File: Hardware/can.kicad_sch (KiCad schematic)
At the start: 9 parts, among them U2 SN65HVD230

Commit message: Crosshair V1.0
New pyro connectors, silkscreen sorted, mostly connected properly + cool new name and image
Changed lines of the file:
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@@
 (kicad_sch
-	(version 20231120)
+	(version 20250114)
 	(generator "eeschema")
-	(generator_version "8.0")
+	(generator_version "9.0")
 	(paper "A4")
 	(junction
@@
 	(label "Vref"
 		(at 124.46 90.17 180)
-		(fields_autoplaced yes)
 		(effects
 			(font
@@
 	(label "Vref"
 		(at 153.67 88.9 180)
-		(fields_autoplaced yes)
 		(effects
 			(font
@@
 		(shape input)
 		(at 111.76 87.63 180)
-		(fields_autoplaced yes)
 		(effects
 			(font
@@
 		(shape bidirectional)
 		(at 175.26 80.01 0)
-		(fields_autoplaced yes)
 		(effects
 			(font
@@
 		(shape output)
 		(at 111.76 85.09 180)
-		(fields_autoplaced yes)
 		(effects
 			(font
@@
 		(shape bidirectional)
 		(at 190.5 97.79 0)
-		(fields_autoplaced yes)
 		(effects
 			(font
@@
 		(shape bidirectional)
 		(at 190.5 80.01 0)
-		(fields_autoplaced yes)
 		(effects
 			(font
@@
 		(shape bidirectional)
 		(at 175.26 97.79 0)
-		(fields_autoplaced yes)
-		(effects
-			(font
+		(effects
+			(font

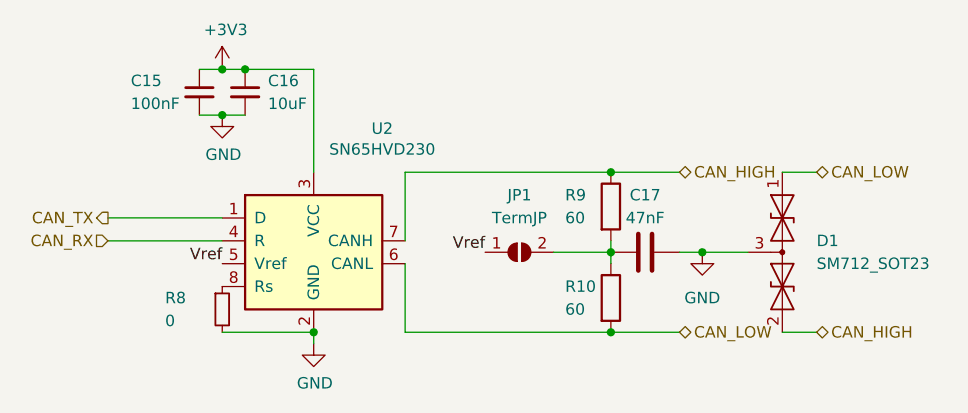
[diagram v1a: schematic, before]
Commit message: More V2 changes
Mainly changed to use Ω symbol for resistors. Fixed the CDC pin for the buck boost
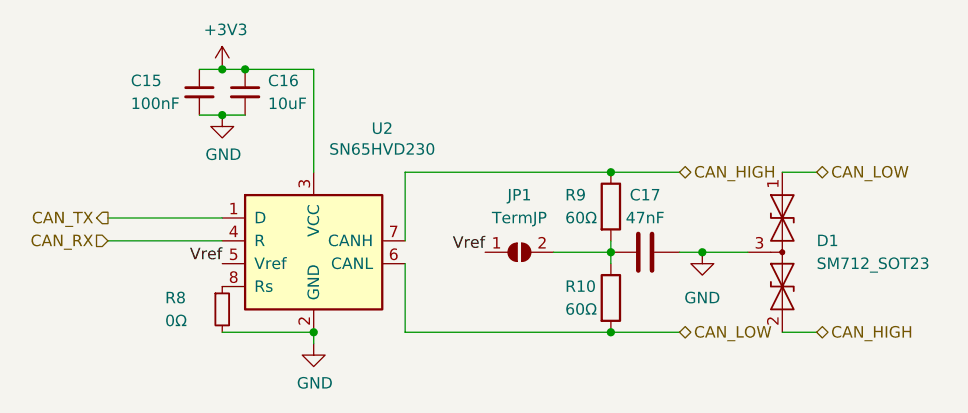
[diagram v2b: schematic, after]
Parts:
- R10, R9: value 60 -> 60Ω
- R8: value 0 -> 0Ω
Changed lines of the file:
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@@
 			)
 		)
-		(property "Value" "0"
+		(property "Value" "0Ω"
 			(at 118.11 96.52 0)
 			(effects
@@
 			)
 		)
-		(property "Value" "60"
+		(property "Value" "60Ω"
 			(at 162.56 95.25 0)
 			(effects
@@
 			)
 		)
-		(property "Value" "60"
+		(property "Value" "60Ω"
 			(at 162.56 85.09 0)
 			(effects

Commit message: reformatted and renamed file
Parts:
- JP701: renamed from JP1; now left out of the parts list
- renumbered C15 to C701, C16 to C702, C17 to C703, D1 to D701, R8 to R701, R9 to R702, R10 to R703, U2 to U701
